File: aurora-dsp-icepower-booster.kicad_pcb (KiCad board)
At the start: 2 copper layers, 180 x 200 mm, 239 parts, among them J1 XLR_IN_1, J10 XLR3_OUT, J11 XLR3_OUT, J12 XLR3_OUT, J13 24V DC, J14 REMOTE 3.5mm, J2 XLR_IN_2, J3 XLR_IN_3, J4 XLR_IN_4, J5 XLR_IN_5, J6 XLR_IN_6, J7 XLR3_OUT, J8 XLR3_OUT, J9 XLR3_OUT, SW1 Gain CH1, SW2 Gain CH2, SW3 Gain CH3, SW4 Gain CH4, SW5 Gain CH5, SW6 Gain CH6, SW7 ALWAYS/REMOTE, U1 LM4562, U10 LM4562, U11 LM4562, U12 LM4562, U13 TEL5-2422, U14 ADP7118ARDZ-11, U15 ADP7182AUJZ-11, U2 LM4562, U3 LM4562, U4 LM4562, U5 LM4562, U6 LM4562, U7 LM4562, U8 LM4562, U9 LM4562

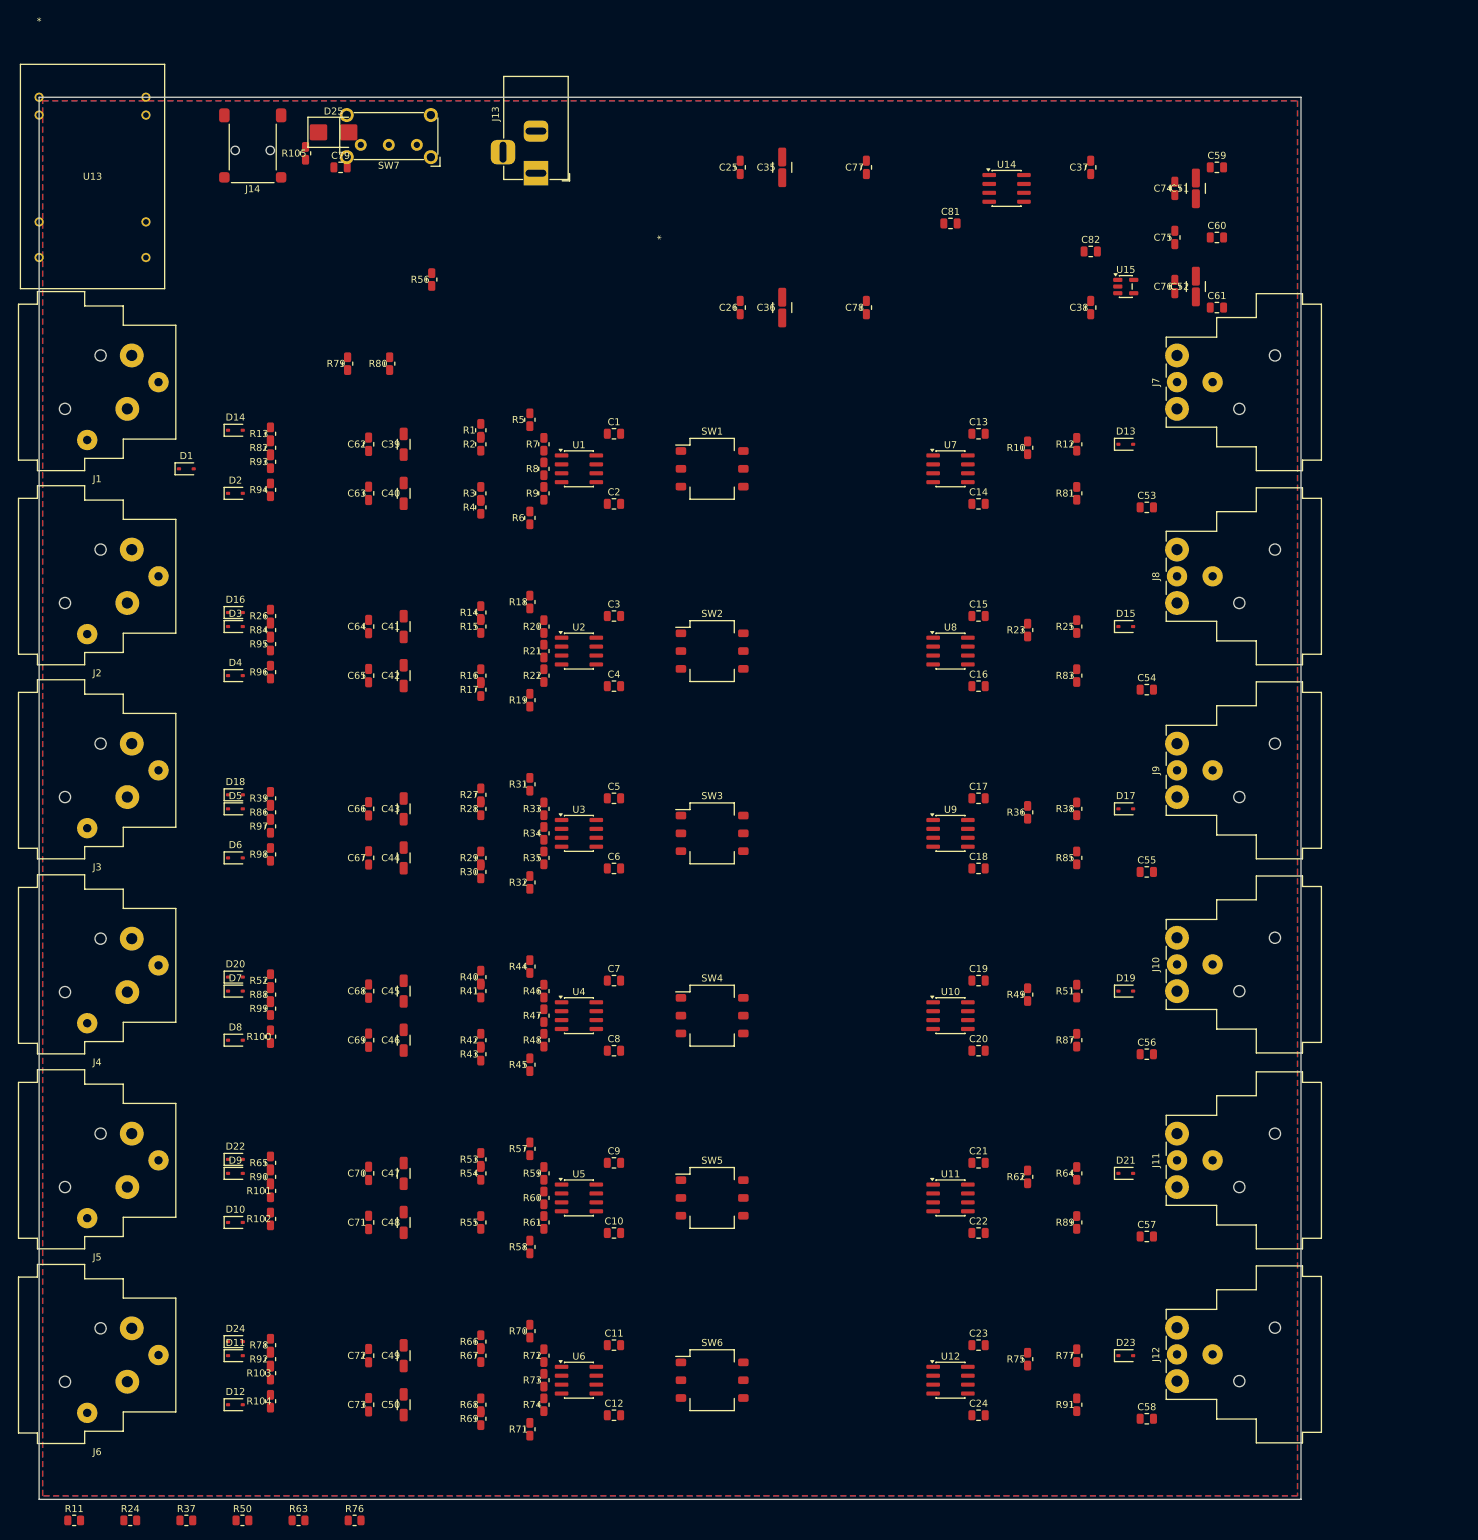
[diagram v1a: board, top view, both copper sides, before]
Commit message: PCB: add build_pcb_v4.py with net-name-driven placement
- 264/264 components placed (0 fallback, 0 skipped)
- Net-name-driven channel+function classification
- Correct netlist refs: J1=barrel, J2=remote, J3-J8=XLR-in,
  J9-J14=XLR-out, SW1=ALWAYS/REMOTE (was wrong in v3)
- U1=TEL5-2422 (was U13 in v3), U14=ADP7118, U15=ADP7182
- IC rules prioritized before passive pattern matching
- Extra .kicad_mod footprints: injection fix for unquoted refs
- DRC: 0 shorts, 18 courtyard/clearance (power zone), 499 unconnected
  (ready for Freerouting)
- Board: 180x200mm, MH1-MH4 mounting holes at corners
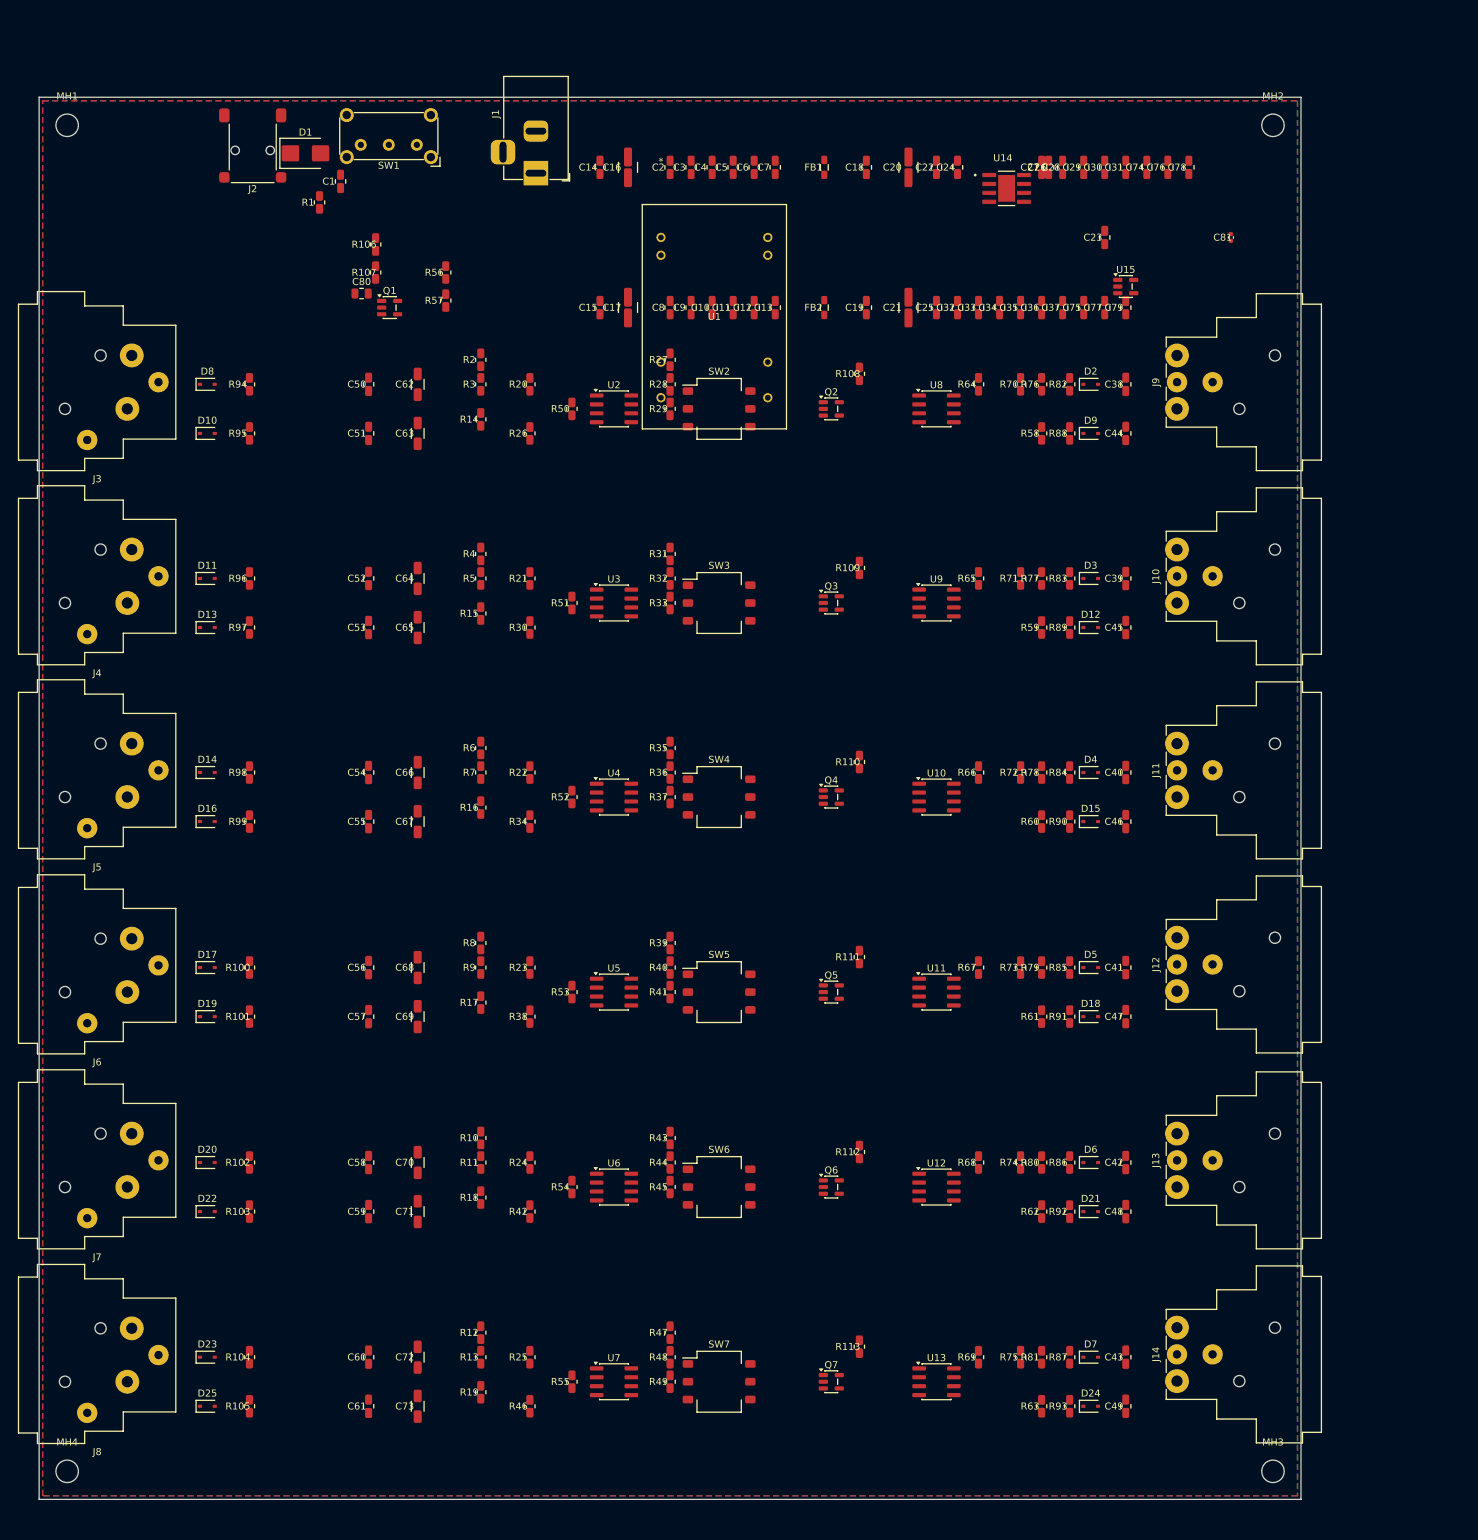
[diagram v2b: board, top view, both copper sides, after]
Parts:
- removed C82: 100nF C0G, Capacitor_SMD:C_0805_2012Metric
- added C27: 100nF C0G, Capacitor_SMD:C_0805_2012Metric, F.Cu at (143.0, 10.0)
- added C28: 100nF C0G, Capacitor_SMD:C_0805_2012Metric, F.Cu at (146.0, 10.0)
- added C29: 100nF C0G, Capacitor_SMD:C_0805_2012Metric, F.Cu at (149.0, 10.0)
- added C30: 100nF C0G, Capacitor_SMD:C_0805_2012Metric, F.Cu at (152.0, 10.0)
- added C31: 100nF C0G, Capacitor_SMD:C_0805_2012Metric, F.Cu at (155.0, 10.0)
- added C32: 100nF C0G, Capacitor_SMD:C_0805_2012Metric, F.Cu at (131.0, 30.0)
- added C33: 100nF C0G, Capacitor_SMD:C_0805_2012Metric, F.Cu at (134.0, 30.0)
- added C34: 100nF C0G, Capacitor_SMD:C_0805_2012Metric, F.Cu at (137.0, 30.0)
- added C80: 10u, Capacitor_SMD:C_0805_2012Metric, F.Cu at (46.0, 28.0)
- added FB1: BLM18PG221, L_0805_2012Metric, F.Cu at (112.0, 10.0)
- added FB2: BLM18PG221, L_0805_2012Metric, F.Cu at (112.0, 30.0)
- added MH1: MountingHole, MountingHole_3.2mm_M3, F.Cu at (4.00, 4.00)
- added MH2: MountingHole, MountingHole_3.2mm_M3, F.Cu at (176.0, 4.00)
- added MH3: MountingHole, MountingHole_3.2mm_M3, F.Cu at (176.0, 196.0)
- added MH4: MountingHole, MountingHole_3.2mm_M3, F.Cu at (4.00, 196.0)
- added Q1: BSS138, Package_TO_SOT_SMD:SOT-23-5, F.Cu at (50.0, 30.0)
- added Q2: BSS138, Package_TO_SOT_SMD:SOT-23-5, F.Cu at (113.0, 44.5)
- added Q3: BSS138, Package_TO_SOT_SMD:SOT-23-5, F.Cu at (113.0, 72.1)
- added Q4: BSS138, Package_TO_SOT_SMD:SOT-23-5, F.Cu at (113.0, 99.8)
- added Q5: BSS138, Package_TO_SOT_SMD:SOT-23-5, F.Cu at (113.0, 127.6)
- added Q6: BSS138, Package_TO_SOT_SMD:SOT-23-5, F.Cu at (113.0, 155.4)
- added Q7: BSS138, Package_TO_SOT_SMD:SOT-23-5, F.Cu at (113.0, 183.2)
- added R106: 10k, Resistor_SMD:R_0805_2012Metric, F.Cu at (48.0, 21.0)
- added R107: 100k, Resistor_SMD:R_0805_2012Metric, F.Cu at (48.0, 25.0)
- added R108: 10k, Resistor_SMD:R_0805_2012Metric, F.Cu at (117.0, 39.5)
- added R109: 10k, Resistor_SMD:R_0805_2012Metric, F.Cu at (117.0, 67.1)
- added R110: 10k, Resistor_SMD:R_0805_2012Metric, F.Cu at (117.0, 94.8)
- added R111: 10k, Resistor_SMD:R_0805_2012Metric, F.Cu at (117.0, 122.6)
- added R112: 10k, Resistor_SMD:R_0805_2012Metric, F.Cu at (117.0, 150.4)
- added R113: 10k, Resistor_SMD:R_0805_2012Metric, F.Cu at (117.0, 178.2)
- C16, C17: value 100nF C0G -> 100uF/25V; footprint Capacitor_SMD:C_0805_2012Metric -> Capacitor_SMD:C_1210_3225Metric
- C20, C21: value 100nF C0G -> 100uF; footprint Capacitor_SMD:C_0805_2012Metric -> Capacitor_SMD:C_1210_3225Metric
- C24, C25, C77, C78, C79: value 100nF C0G -> 10uF X5R
- C35, C36: value 100uF/25V -> 100nF C0G; footprint Capacitor_SMD:C_1210_3225Metric -> Capacitor_SMD:C_0805_2012Metric
- C37, C38: value 10uF X5R -> 100nF C0G
- C39, C40, C41, C42, C43, C44, C45, C46, C47, C48, C49: value 2.2uF C0G -> 100nF C0G; footprint Capacitor_SMD:C_1206_3216Metric -> Capacitor_SMD:C_0805_2012Metric
- C50: value 2.2uF C0G -> 100pF C0G; footprint Capacitor_SMD:C_1206_3216Metric -> Capacitor_SMD:C_0805_2012Metric
- C51, C52: value 100uF -> 100pF C0G; footprint Capacitor_SMD:C_1210_3225Metric -> Capacitor_SMD:C_0805_2012Metric
- C53, C54, C55, C56, C57, C58, C59, C60, C61: value 100nF C0G -> 100pF C0G
- C62, C63, C64: value 100nF C0G -> 2.2uF C0G; footprint Capacitor_SMD:C_0805_2012Metric -> Capacitor_SMD:C_1206_3216Metric
- C65, C66, C67, C68, C69, C70, C71, C72, C73: value 100pF C0G -> 2.2uF C0G; footprint Capacitor_SMD:C_0805_2012Metric -> Capacitor_SMD:C_1206_3216Metric
- C74, C75, C76: value 100pF C0G -> 10uF X5R
- C81: value 100nF C0G -> 22nF C0G; footprint Capacitor_SMD:C_0805_2012Metric -> C_0402_1005Metric
- D1: value PESD5V0S1BL -> SMBJ15CA; footprint Diode_SMD:D_SOD-323 -> Diode_SMD:D_SMB
- D25: value SMBJ15CA -> PESD5V0S1BL; footprint Diode_SMD:D_SMB -> Diode_SMD:D_SOD-323
- J1: value XLR_IN_1 -> 24V DC; footprint Connector_Audio:Jack_XLR_Neutrik_NC3FBH2_Horizontal -> Connector_BarrelJack:BarrelJack_Horizontal
- J13: value 24V DC -> XLR3_OUT; footprint Connector_BarrelJack:BarrelJack_Horizontal -> Connector_Audio:Jack_XLR_Neutrik_NC3MBH_Horizontal
- J14: value REMOTE 3.5mm -> XLR3_OUT; footprint Connector_Audio:Jack_3.5mm_Lumberg_1503_02_Horizontal -> Connector_Audio:Jack_XLR_Neutrik_NC3MBH_Horizontal
- J2: value XLR_IN_2 -> REMOTE 3.5mm; footprint Connector_Audio:Jack_XLR_Neutrik_NC3FBH2_Horizontal -> Connector_Audio:Jack_3.5mm_Lumberg_1503_02_Horizontal
- J3: value XLR_IN_3 -> XLR_IN_1
- J4: value XLR_IN_4 -> XLR_IN_2
- J5: value XLR_IN_5 -> XLR_IN_3
- J6: value XLR_IN_6 -> XLR_IN_4
- J7: value XLR3_OUT -> XLR_IN_5; footprint Connector_Audio:Jack_XLR_Neutrik_NC3MBH_Horizontal -> Connector_Audio:Jack_XLR_Neutrik_NC3FBH2_Horizontal
- J8: value XLR3_OUT -> XLR_IN_6; footprint Connector_Audio:Jack_XLR_Neutrik_NC3MBH_Horizontal -> Connector_Audio:Jack_XLR_Neutrik_NC3FBH2_Horizontal
- R1, R66, R67, R68, R69, R70, R71: value 10k 0.1% -> 10k
- R10, R11, R23, R24, R50: value 10k -> 10k 0.1%
- R105, R62, R63, R76: value 10k -> 47
- R12, R13, R25, R26, R38, R51, R52: value 47 -> 10k 0.1%
- R20, R46, R7: value 30k -> 10k 0.1%
- R21, R34, R8: value 15k -> 10k 0.1%
- R22, R9: value 7.5k -> 10k 0.1%
- R27, R31, R43: value 10k 0.1% -> 30k
- R28, R32, R40, R44: value 10k 0.1% -> 15k
- R29, R41, R45: value 10k 0.1% -> 7.5k
- R33: value 30k -> 7.5k
- R35: value 7.5k -> 30k
- R36: value 10k -> 15k
- R37, R49: value 10k -> 7.5k
- R39: value 47 -> 30k
- R47: value 15k -> 30k
- R48: value 7.5k -> 15k
- R56, R57: value 10k 0.1% -> 100k
- R58: value 10k 0.1% -> 47
- R59: value 30k -> 47
- R60: value 15k -> 47
- R61: value 7.5k -> 47
- R64, R65: value 47 -> 10k
- R72: value 30k -> 10k
- R73: value 15k -> 10k
- R74: value 7.5k -> 10k
- R79, R80: value 100k -> 47
- R81: value 10 -> 47
- R93: value 47 -> 10
- SW1: value Gain CH1 -> ALWAYS/REMOTE; footprint Button_Switch_SMD:SW_DIP_SPSTx03_Slide_Omron_A6S-310x_W8.9mm_P2.54mm -> Button_Switch_THT:SW_E-Switch_EG1224_SPDT_Angled
- SW2: value Gain CH2 -> Gain CH1
- SW3: value Gain CH3 -> Gain CH2
- SW4: value Gain CH4 -> Gain CH3
- SW5: value Gain CH5 -> Gain CH4
- SW6: value Gain CH6 -> Gain CH5
- SW7: value ALWAYS/REMOTE -> Gain CH6; footprint Button_Switch_THT:SW_E-Switch_EG1224_SPDT_Angled -> Button_Switch_SMD:SW_DIP_SPSTx03_Slide_Omron_A6S-310x_W8.9mm_P2.54mm
- U1: value LM4562 -> TEL5-2422; footprint Package_SO:SOIC-8_3.9x4.9mm_P1.27mm -> TEL5_DUAL_TRP
- U13: value TEL5-2422 -> LM4562; footprint TEL5_DUAL_TRP -> Package_SO:SOIC-8_3.9x4.9mm_P1.27mm
- U14: footprint Package_SO:SOIC-8_3.9x4.9mm_P1.27mm -> SOIC127P600X175-9N
- moved U13 223.5 mm to (128.0, 183.2)
- moved J14 221.5 mm to (162.3, 183.1), turned to 90 degrees
- moved C60 200.4 mm to (47.0, 179.7), turned to 90 degrees
- moved C61 198.0 mm to (47.0, 186.7), turned to 90 degrees
- moved C59 191.9 mm to (47.0, 158.9), turned to 90 degrees
- moved R76 189.4 mm to (143.0, 41.0), turned to 90 degrees
- moved J8 186.4 mm to (12.6, 183.2), turned to 180 degrees
- moved J7 186.4 mm to (12.6, 155.4), turned to 180 degrees
- moved D25 182.6 mm to (24.0, 186.7)
- moved SW7 181.6 mm to (97.0, 183.2), turned to 0 degrees
- moved R105 178.9 mm to (30.0, 186.7)
- moved C24 178.0 mm to (131.0, 10.0), turned to 90 degrees
- moved R93 176.5 mm to (147.0, 186.7)
- moved J13 171.1 mm to (162.3, 155.4), turned to 90 degrees
- moved R50 165.4 mm to (76.0, 44.5), turned to 90 degrees
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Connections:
- C1 pad 1: /GND -> /REMOTE_FILT
- C1 pad 2: /V+ -> GND
- C10 pad 1: /GND -> GND
- C11 pad 1: /GND -> GND
- C11 pad 2: /V+ -> /V-
- C12 pad 1: /V- -> GND
- C12 pad 2: /GND -> /V-
- C13 pad 1: /GND -> GND
- C13 pad 2: /V+ -> /V-
- C14 pad 1: /GND -> GND
- C14 pad 2: /V- -> /+12V_RAW
- C15 pad 1: /GND -> /-12V_RAW
- C15 pad 2: /V+ -> GND
- C16 pad 1: /V- -> GND
- C16 pad 2: /GND -> /+12V_RAW
- C17 pad 1: /GND -> /-12V_RAW
- C17 pad 2: /V+ -> GND
- C18 pad 1: /GND -> GND
- C18 pad 2: /V- -> /+12V
- C19 pad 1: /GND -> /-12V
- C19 pad 2: /V+ -> GND
- C2 pad 1: /GND -> GND
- C2 pad 2: /V- -> /V+
- C20 pad 1: /V- -> GND
- C20 pad 2: /GND -> /V+
- C21 pad 1: /GND -> /V-
- C21 pad 2: /V+ -> GND
- C22 pad 1: /GND -> /V+
- C22 pad 2: /V- -> GND
- C23 pad 1: /GND -> /NR_U15
- C23 pad 2: /V+ -> GND
- C24 pad 1: /V- -> GND
- C24 pad 2: /GND -> /V+
- C25 pad 1: /GND -> /V-
- C25 pad 2: /+12V -> GND
- C26 pad 1: /-12V -> GND
- C26 pad 2: /GND -> /V+
- C3 pad 1: /GND -> GND
- C35 pad 1: /GND -> /V-
- C35 pad 2: /+12V -> GND
- C36 pad 1: /-12V -> /V-
- C36 pad 2: /GND -> GND
- C37 pad 1: /GND -> /V-
- C37 pad 2: /V+ -> GND
- C38 pad 1: /V- -> /CH1_OUT_PROT_HOT
- C38 pad 2: /GND -> GND
- C39 pad 1: (no net) -> /CH2_OUT_PROT_HOT
- C39 pad 2: /CH1_HOT_IN -> GND
- C4 pad 1: /V- -> GND
- C4 pad 2: /GND -> /V+
- C40 pad 1: (no net) -> /CH3_OUT_PROT_HOT
- C40 pad 2: /CH1_COLD_IN -> GND
- C41 pad 1: (no net) -> /CH4_OUT_PROT_HOT
- C41 pad 2: /CH2_HOT_IN -> GND
- C42 pad 1: (no net) -> /CH5_OUT_PROT_HOT
- C42 pad 2: /CH2_COLD_IN -> GND
- C43 pad 1: (no net) -> /CH6_OUT_PROT_HOT
- C43 pad 2: /CH3_HOT_IN -> GND
- C44 pad 1: (no net) -> /CH1_OUT_PROT_COLD
- C44 pad 2: /CH3_COLD_IN -> GND
- C45 pad 1: (no net) -> /CH2_OUT_PROT_COLD
- C45 pad 2: /CH4_HOT_IN -> GND
- C46 pad 1: (no net) -> /CH3_OUT_PROT_COLD
- C46 pad 2: /CH4_COLD_IN -> GND
- C47 pad 1: (no net) -> /CH4_OUT_PROT_COLD
- C47 pad 2: /CH5_HOT_IN -> GND
- C48 pad 1: (no net) -> /CH5_OUT_PROT_COLD
- C48 pad 2: /CH5_COLD_IN -> GND
- C49 pad 1: (no net) -> /CH6_OUT_PROT_COLD
- C49 pad 2: /CH6_HOT_IN -> GND
- C5 pad 1: /GND -> GND
- C50 pad 1: (no net) -> /CH1_EMI_HOT
- C50 pad 2: /CH6_COLD_IN -> GND
- C51 pad 1: /GND -> /CH1_EMI_COLD
- C51 pad 2: /GND -> GND
- C52 pad 1: /GND -> /CH2_EMI_HOT
- C52 pad 2: /GND -> GND
- C53 pad 1: (no net) -> /CH2_EMI_COLD
- C53 pad 2: /GND -> GND
- C54 pad 1: (no net) -> /CH3_EMI_HOT
- C54 pad 2: /GND -> GND
- C55 pad 1: (no net) -> /CH3_EMI_COLD
- C55 pad 2: /GND -> GND
- C56 pad 1: (no net) -> /CH4_EMI_HOT
- C56 pad 2: /GND -> GND
- C57 pad 1: (no net) -> /CH4_EMI_COLD
- C57 pad 2: /GND -> GND
- C58 pad 1: (no net) -> /CH5_EMI_HOT
- C58 pad 2: /GND -> GND
- C59 pad 1: (no net) -> /CH5_EMI_COLD
- C59 pad 2: /GND -> GND
- C6 pad 1: /GND -> GND
- C6 pad 2: /V- -> /V+
- C60 pad 1: (no net) -> /CH6_EMI_HOT
- C60 pad 2: /GND -> GND
- C61 pad 1: (no net) -> /CH6_EMI_COLD
- C61 pad 2: /GND -> GND
- C62 pad 1: (no net) -> /CH1_EMI_HOT
- C62 pad 2: /GND -> /CH1_HOT_IN
- C63 pad 1: (no net) -> /CH1_EMI_COLD
- C63 pad 2: /GND -> /CH1_COLD_IN
- C64 pad 1: (no net) -> /CH2_EMI_HOT
- C64 pad 2: /GND -> /CH2_HOT_IN
- C65 pad 1: (no net) -> /CH2_EMI_COLD
- C65 pad 2: /GND -> /CH2_COLD_IN
- C66 pad 1: (no net) -> /CH3_EMI_HOT
- C66 pad 2: /GND -> /CH3_HOT_IN
- C67 pad 1: (no net) -> /CH3_EMI_COLD
- C67 pad 2: /GND -> /CH3_COLD_IN
- C68 pad 1: (no net) -> /CH4_EMI_HOT
- C68 pad 2: /GND -> /CH4_HOT_IN
- C69 pad 1: (no net) -> /CH4_EMI_COLD
- C69 pad 2: /GND -> /CH4_COLD_IN
- C7 pad 1: /GND -> GND
- C70 pad 1: (no net) -> /CH5_EMI_HOT
- C70 pad 2: /GND -> /CH5_HOT_IN
- C71 pad 1: (no net) -> /CH5_EMI_COLD
- C71 pad 2: /GND -> /CH5_COLD_IN
- C72 pad 1: (no net) -> /CH6_EMI_HOT
- C72 pad 2: /GND -> /CH6_HOT_IN
- C73 pad 1: (no net) -> /CH6_EMI_COLD
- C73 pad 2: /GND -> /CH6_COLD_IN
- C74 pad 1: (no net) -> GND
- C74 pad 2: /GND -> /V+
- C75 pad 1: (no net) -> /V-
- C75 pad 2: /GND -> GND
- C76 pad 1: (no net) -> GND
- C76 pad 2: /GND -> /V+
- C77 pad 1: /GND -> /V-
- C77 pad 2: /+12V -> GND
- C78 pad 1: /-12V -> GND
- C78 pad 2: /GND -> /V+
- C79 pad 1: /REMOTE_FILT -> /V-
- C79 pad 2: /GND -> GND
- C8 pad 1: /V- -> GND
- C8 pad 2: /GND -> /V-
- C81 pad 2: /GND -> GND
- C9 pad 1: /GND -> GND
- C9 pad 2: /V+ -> /V-
- D1 pad 1: /GND -> /REMOTE_IN
- D1 pad 2: /CH1_HOT_RAW -> GND
- D10 pad 1: /GND -> GND
- D10 pad 2: /CH5_COLD_RAW -> /CH1_COLD_RAW
- D11 pad 1: /GND -> GND
- D11 pad 2: /CH6_HOT_RAW -> /CH2_HOT_RAW
- D12 pad 1: /GND -> GND
- D12 pad 2: /CH6_COLD_RAW -> /CH2_OUT_COLD
- D13 pad 1: /GND -> GND
- D13 pad 2: /CH1_OUT_HOT -> /CH2_COLD_RAW
- D14 pad 1: /GND -> GND
- D14 pad 2: /CH1_HOT_RAW -> /CH3_HOT_RAW
- D15 pad 1: /GND -> GND
- D15 pad 2: /CH2_OUT_HOT -> /CH3_OUT_COLD
- D16 pad 1: /GND -> GND
- D16 pad 2: /CH2_HOT_RAW -> /CH3_COLD_RAW
- D17 pad 1: /GND -> GND
- D17 pad 2: /CH3_OUT_HOT -> /CH4_HOT_RAW
- D18 pad 1: /GND -> GND
- D18 pad 2: /CH3_HOT_RAW -> /CH4_OUT_COLD
- D19 pad 1: /GND -> GND
- D19 pad 2: /CH4_OUT_HOT -> /CH4_COLD_RAW
- D2 pad 1: /GND -> GND
- D2 pad 2: /CH1_COLD_RAW -> /CH1_OUT_HOT
- D20 pad 1: /GND -> GND
- D20 pad 2: /CH4_HOT_RAW -> /CH5_HOT_RAW
- D21 pad 1: /GND -> GND
- D21 pad 2: /CH5_OUT_HOT -> /CH5_OUT_COLD
- D22 pad 1: /GND -> GND
- D22 pad 2: /CH5_HOT_RAW -> /CH5_COLD_RAW
- D23 pad 1: /GND -> GND
- D23 pad 2: /CH6_OUT_HOT -> /CH6_HOT_RAW
- D24 pad 1: /GND -> GND
- D24 pad 2: /CH6_HOT_RAW -> /CH6_OUT_COLD
- D25 pad 1: /REMOTE_IN -> GND
- D25 pad 2: /GND -> /CH6_COLD_RAW
- D3 pad 1: /GND -> GND
- D3 pad 2: /CH2_HOT_RAW -> /CH2_OUT_HOT
- D4 pad 1: /GND -> GND
- D4 pad 2: /CH2_COLD_RAW -> /CH3_OUT_HOT
- D5 pad 1: /GND -> GND
- D5 pad 2: /CH3_HOT_RAW -> /CH4_OUT_HOT
- D6 pad 1: /GND -> GND
- D6 pad 2: /CH3_COLD_RAW -> /CH5_OUT_HOT
- D7 pad 1: /GND -> GND
- D7 pad 2: /CH4_HOT_RAW -> /CH6_OUT_HOT
- D8 pad 1: /GND -> GND
- D8 pad 2: /CH4_COLD_RAW -> /CH1_HOT_RAW
- D9 pad 1: /GND -> GND
- D9 pad 2: /CH5_HOT_RAW -> /CH1_OUT_COLD
- J1 pad 1: /GND -> /+24V_IN
- J1 pad 2: /CH1_HOT_RAW -> GND
- J10 pad 1: /GND -> GND
- J10 pad 2: /CH4_OUT_HOT -> /CH2_OUT_HOT
- J10 pad 3: (no net) -> /CH2_OUT_COLD
- J11 pad 1: /GND -> GND
- J11 pad 2: /CH5_OUT_HOT -> /CH3_OUT_HOT
- J11 pad 3: (no net) -> /CH3_OUT_COLD
- J12 pad 1: /GND -> GND
- J12 pad 2: /CH6_OUT_HOT -> /CH4_OUT_HOT
- J12 pad 3: (no net) -> /CH4_OUT_COLD
- J13 pad 1: /+24V_IN -> GND
- J13 pad 2: /GND -> /CH5_OUT_HOT
- J13 pad 3: (no net) -> /CH5_OUT_COLD
- J3 pad 1: /GND -> GND
- J3 pad 2: /CH3_HOT_RAW -> /CH1_HOT_RAW
- J3 pad 3: (no net) -> /CH1_COLD_RAW
- J3 pad G: (no net) -> GND
- J4 pad 1: /GND -> GND
- J4 pad 2: /CH4_HOT_RAW -> /CH2_HOT_RAW
- J4 pad 3: (no net) -> /CH2_COLD_RAW
- J4 pad G: (no net) -> GND
- J5 pad 1: /GND -> GND
- J5 pad 2: /CH5_HOT_RAW -> /CH3_HOT_RAW
- J5 pad 3: (no net) -> /CH3_COLD_RAW
- J5 pad G: (no net) -> GND
- J6 pad 1: /GND -> GND
- J6 pad 2: /CH6_HOT_RAW -> /CH4_HOT_RAW
- J6 pad 3: (no net) -> /CH4_COLD_RAW
- J6 pad G: (no net) -> GND
- J7 pad 1: /GND -> GND
- J7 pad 2: /CH1_OUT_HOT -> /CH5_HOT_RAW
- J7 pad 3: (no net) -> /CH5_COLD_RAW
- J7 pad G: (no net) -> GND
- J8 pad 1: /GND -> GND
- J8 pad 2: /CH2_OUT_HOT -> /CH6_HOT_RAW
- J8 pad 3: (no net) -> /CH6_COLD_RAW
- J8 pad G: (no net) -> GND
- J9 pad 1: /GND -> GND
- J9 pad 2: /CH3_OUT_HOT -> /CH1_OUT_HOT
- J9 pad 3: (no net) -> /CH1_OUT_COLD
- R1 pad 1: (no net) -> /REMOTE_IN
- R1 pad 2: /CH1_HOT_IN -> /REMOTE_FILT
- R10 pad 1: (no net) -> GND
- R10 pad 2: /CH1_GAIN_OUT -> /CH5_HOT_IN
- R100 pad 1: /CH4_COLD_RAW -> /CH4_HOT_RAW
- R100 pad 2: (no net) -> /CH4_EMI_HOT
- R101 pad 1: /CH5_HOT_RAW -> /CH4_COLD_RAW
- R101 pad 2: (no net) -> /CH4_EMI_COLD
- R102 pad 1: /CH5_COLD_RAW -> /CH5_HOT_RAW
- R102 pad 2: (no net) -> /CH5_EMI_HOT
- R103 pad 1: /CH6_HOT_RAW -> /CH5_COLD_RAW
- R103 pad 2: (no net) -> /CH5_EMI_COLD
- R104 pad 1: /CH6_COLD_RAW -> /CH6_HOT_RAW
- R104 pad 2: (no net) -> /CH6_EMI_HOT
- R105 pad 1: /REMOTE_IN -> /CH6_COLD_RAW
- R105 pad 2: /REMOTE_FILT -> /CH6_EMI_COLD
- R11 pad 1: (no net) -> /CH5_INV_IN
- R11 pad 2: (no net) -> /CH5_COLD_IN
- R12 pad 1: (no net) -> GND
- R12 pad 2: /CH1_OUT_HOT -> /CH6_HOT_IN
- R13 pad 1: (no net) -> /CH6_INV_IN
- R13 pad 2: /CH1_HOT_RAW -> /CH6_COLD_IN
- R14 pad 1: /CH2_HOT_IN -> GND
- R14 pad 2: /CH2_HOT_IN -> /CH1_INV_IN
- R15 pad 1: /CH2_HOT_IN -> GND
- R15 pad 2: (no net) -> /CH2_INV_IN
- R16 pad 1: (no net) -> GND
- R16 pad 2: /CH2_COLD_IN -> /CH3_INV_IN
- R17 pad 1: /GND -> GND
- R17 pad 2: (no net) -> /CH4_INV_IN
- R18 pad 1: /CH2_SUMNODE -> GND
- R18 pad 2: /CH2_RX_OUT -> /CH5_INV_IN
- R19 pad 1: /CH2_SUMNODE -> GND
- R19 pad 2: /CH2_GAIN_OUT -> /CH6_INV_IN
- R2 pad 1: /CH1_HOT_IN -> GND
- R2 pad 2: (no net) -> /CH1_HOT_IN
- R20 pad 1: (no net) -> /CH1_INV_IN
- R20 pad 2: /CH2_SUMNODE -> /CH1_RX_OUT
- R21 pad 1: (no net) -> /CH2_INV_IN
- R21 pad 2: /CH2_SUMNODE -> /CH2_RX_OUT
- R22 pad 1: (no net) -> /CH3_INV_IN
- R22 pad 2: /CH2_SUMNODE -> /CH3_RX_OUT
- R23 pad 1: (no net) -> /CH4_INV_IN
- R23 pad 2: /CH2_GAIN_OUT -> /CH4_RX_OUT
- R24 pad 1: (no net) -> /CH5_INV_IN
- R24 pad 2: (no net) -> /CH5_RX_OUT
- R25 pad 1: (no net) -> /CH6_INV_IN
- R25 pad 2: /CH2_OUT_HOT -> /CH6_RX_OUT
- R26 pad 1: (no net) -> /CH1_SUMNODE
- R26 pad 2: /CH2_HOT_RAW -> /CH1_RX_OUT
- R27 pad 1: /CH3_HOT_IN -> /CH1_SW_OUT_1
- R27 pad 2: /CH3_HOT_IN -> /CH1_SUMNODE
- R28 pad 1: /CH3_HOT_IN -> /CH1_SW_OUT_2
- R28 pad 2: (no net) -> /CH1_SUMNODE
- R29 pad 1: (no net) -> /CH1_SW_OUT_3
- R29 pad 2: /CH3_COLD_IN -> /CH1_SUMNODE
- R3 pad 1: (no net) -> /CH1_INV_IN
- R30 pad 1: /GND -> /CH2_SUMNODE
- R30 pad 2: (no net) -> /CH2_RX_OUT
- R31 pad 1: /CH3_SUMNODE -> /CH2_SW_OUT_1
- R31 pad 2: /CH3_RX_OUT -> /CH2_SUMNODE
- R32 pad 1: /CH3_SUMNODE -> /CH2_SW_OUT_2
- R32 pad 2: /CH3_GAIN_OUT -> /CH2_SUMNODE
- R33 pad 1: (no net) -> /CH2_SW_OUT_3
- R33 pad 2: /CH3_SUMNODE -> /CH2_SUMNODE
- R34 pad 1: (no net) -> /CH3_SUMNODE
- R34 pad 2: /CH3_SUMNODE -> /CH3_RX_OUT
- R35 pad 1: (no net) -> /CH3_SW_OUT_1
- R36 pad 1: (no net) -> /CH3_SW_OUT_2
- R36 pad 2: /CH3_GAIN_OUT -> /CH3_SUMNODE
- R37 pad 1: (no net) -> /CH3_SW_OUT_3
- R37 pad 2: (no net) -> /CH3_SUMNODE
- R38 pad 1: (no net) -> /CH4_SUMNODE
- R38 pad 2: /CH3_OUT_HOT -> /CH4_RX_OUT
- R39 pad 1: (no net) -> /CH4_SW_OUT_1
- R39 pad 2: /CH3_HOT_RAW -> /CH4_SUMNODE
- R4 pad 1: /GND -> GND
- R4 pad 2: (no net) -> /CH2_HOT_IN
- R40 pad 1: /CH4_HOT_IN -> /CH4_SW_OUT_2
- R40 pad 2: /CH4_HOT_IN -> /CH4_SUMNODE
- R41 pad 1: /CH4_HOT_IN -> /CH4_SW_OUT_3
- R41 pad 2: (no net) -> /CH4_SUMNODE
- R42 pad 1: (no net) -> /CH5_SUMNODE
- R42 pad 2: /CH4_COLD_IN -> /CH5_RX_OUT
- R43 pad 1: /GND -> /CH5_SW_OUT_1
- R43 pad 2: (no net) -> /CH5_SUMNODE
- R44 pad 1: /CH4_SUMNODE -> /CH5_SW_OUT_2
- R44 pad 2: /CH4_RX_OUT -> /CH5_SUMNODE
- R45 pad 1: /CH4_SUMNODE -> /CH5_SW_OUT_3
- R45 pad 2: /CH4_GAIN_OUT -> /CH5_SUMNODE
- R46 pad 1: (no net) -> /CH6_SUMNODE
- R46 pad 2: /CH4_SUMNODE -> /CH6_RX_OUT
- R47 pad 1: (no net) -> /CH6_SW_OUT_1
- R47 pad 2: /CH4_SUMNODE -> /CH6_SUMNODE
- R48 pad 1: (no net) -> /CH6_SW_OUT_2
- R48 pad 2: /CH4_SUMNODE -> /CH6_SUMNODE
- R49 pad 1: (no net) -> /CH6_SW_OUT_3
- R49 pad 2: /CH4_GAIN_OUT -> /CH6_SUMNODE
- R5 pad 1: /CH1_SUMNODE -> /CH2_INV_IN
- R5 pad 2: /CH1_RX_OUT -> /CH2_COLD_IN
- R50 pad 1: (no net) -> /CH1_SUMNODE
- R50 pad 2: (no net) -> /CH1_GAIN_OUT
- R51 pad 1: (no net) -> /CH2_SUMNODE
- R51 pad 2: /CH4_OUT_HOT -> /CH2_GAIN_OUT
- R52 pad 1: (no net) -> /CH3_SUMNODE
- R52 pad 2: /CH4_HOT_RAW -> /CH3_GAIN_OUT
- R53 pad 1: /CH5_HOT_IN -> /CH4_SUMNODE
- R53 pad 2: /CH5_HOT_IN -> /CH4_GAIN_OUT
- R54 pad 1: /CH5_HOT_IN -> /CH5_SUMNODE
- R54 pad 2: (no net) -> /CH5_GAIN_OUT
- R55 pad 1: (no net) -> /CH6_SUMNODE
- R55 pad 2: /CH5_COLD_IN -> /CH6_GAIN_OUT
- R56 pad 1: /GND -> /EN_CTRL
- R56 pad 2: (no net) -> /V+
- R57 pad 1: /CH5_SUMNODE -> /EN_CTRL
- R57 pad 2: /CH5_RX_OUT -> GND
- R58 pad 1: /CH5_SUMNODE -> /CH1_BUF_DRIVE
- R58 pad 2: /CH5_GAIN_OUT -> /CH1_OUT_COLD
- R59 pad 1: (no net) -> /CH2_BUF_DRIVE
- R59 pad 2: /CH5_SUMNODE -> /CH2_OUT_COLD
- R6 pad 1: /CH1_SUMNODE -> GND
- R6 pad 2: /CH1_GAIN_OUT -> /CH3_HOT_IN
- R60 pad 1: (no net) -> /CH3_BUF_DRIVE
- R60 pad 2: /CH5_SUMNODE -> /CH3_OUT_COLD
- R61 pad 1: (no net) -> /CH4_BUF_DRIVE
- R61 pad 2: /CH5_SUMNODE -> /CH4_OUT_COLD
- R62 pad 1: (no net) -> /CH5_BUF_DRIVE
- R62 pad 2: /CH5_GAIN_OUT -> /CH5_OUT_COLD
- R63 pad 1: (no net) -> /CH6_BUF_DRIVE
- R63 pad 2: (no net) -> /CH6_OUT_COLD
- R64 pad 1: (no net) -> /CH1_GAIN_FB
- R64 pad 2: /CH5_OUT_HOT -> /CH1_GAIN_OUT
- R65 pad 1: (no net) -> /CH2_GAIN_FB
- R65 pad 2: /CH5_HOT_RAW -> /CH2_GAIN_OUT
- R66 pad 1: /CH6_HOT_IN -> /CH3_GAIN_FB
- R66 pad 2: /CH6_HOT_IN -> /CH3_GAIN_OUT
- R67 pad 1: /CH6_HOT_IN -> /CH4_GAIN_FB
- R67 pad 2: (no net) -> /CH4_GAIN_OUT
- R68 pad 1: (no net) -> /CH5_GAIN_FB
- R68 pad 2: /CH6_COLD_IN -> /CH5_GAIN_OUT
- R69 pad 1: /GND -> /CH6_GAIN_FB
- R69 pad 2: (no net) -> /CH6_GAIN_OUT
- R7 pad 1: (no net) -> /CH3_INV_IN
- R7 pad 2: /CH1_SUMNODE -> /CH3_COLD_IN
- R70 pad 1: /CH6_SUMNODE -> /CH1_GAIN_FB
- R70 pad 2: /CH6_RX_OUT -> /CH1_OUT_DRIVE
- R71 pad 1: /CH6_SUMNODE -> /CH2_GAIN_FB
- R71 pad 2: /CH6_GAIN_OUT -> /CH2_OUT_DRIVE
- R72 pad 1: (no net) -> /CH3_GAIN_FB
- R72 pad 2: /CH6_SUMNODE -> /CH3_OUT_DRIVE
- R73 pad 1: (no net) -> /CH4_GAIN_FB
- R73 pad 2: /CH6_SUMNODE -> /CH4_OUT_DRIVE
- R74 pad 1: (no net) -> /CH5_GAIN_FB
- R74 pad 2: /CH6_SUMNODE -> /CH5_OUT_DRIVE
- R75 pad 1: (no net) -> /CH6_GAIN_FB
- R75 pad 2: /CH6_GAIN_OUT -> /CH6_OUT_DRIVE
- R76 pad 1: (no net) -> /CH1_OUT_DRIVE
- R76 pad 2: (no net) -> /CH1_OUT_HOT
- R77 pad 1: (no net) -> /CH2_OUT_DRIVE
- R77 pad 2: /CH6_OUT_HOT -> /CH2_OUT_HOT
- R78 pad 1: (no net) -> /CH3_OUT_DRIVE
- R78 pad 2: /CH6_HOT_RAW -> /CH3_OUT_HOT
- R79 pad 1: /EN_CTRL -> /CH4_OUT_DRIVE
- R79 pad 2: /GND -> /CH4_OUT_HOT
- R8 pad 1: (no net) -> GND
- R8 pad 2: /CH1_SUMNODE -> /CH4_HOT_IN
- R80 pad 1: /EN_CTRL -> /CH5_OUT_DRIVE
- R80 pad 2: /GND -> /CH5_OUT_HOT
- R81 pad 1: /CH1_OUT_HOT -> /CH6_OUT_DRIVE
- R81 pad 2: (no net) -> /CH6_OUT_HOT
- R82 pad 1: /CH1_HOT_RAW -> /CH1_OUT_HOT
- R82 pad 2: (no net) -> /CH1_OUT_PROT_HOT
- R83 pad 2: (no net) -> /CH2_OUT_PROT_HOT
- R84 pad 1: /CH2_HOT_RAW -> /CH3_OUT_HOT
- R84 pad 2: (no net) -> /CH3_OUT_PROT_HOT
- R85 pad 1: /CH3_OUT_HOT -> /CH4_OUT_HOT
- R85 pad 2: (no net) -> /CH4_OUT_PROT_HOT
- R86 pad 1: /CH3_HOT_RAW -> /CH5_OUT_HOT
- R86 pad 2: (no net) -> /CH5_OUT_PROT_HOT
- R87 pad 1: /CH4_OUT_HOT -> /CH6_OUT_HOT
- R87 pad 2: (no net) -> /CH6_OUT_PROT_HOT
- R88 pad 1: /CH4_HOT_RAW -> /CH1_OUT_COLD
- R88 pad 2: (no net) -> /CH1_OUT_PROT_COLD
- R89 pad 1: /CH5_OUT_HOT -> /CH2_OUT_COLD
- R89 pad 2: (no net) -> /CH2_OUT_PROT_COLD
- R9 pad 1: (no net) -> /CH4_INV_IN
- R9 pad 2: /CH1_SUMNODE -> /CH4_COLD_IN
- R90 pad 1: /CH5_HOT_RAW -> /CH3_OUT_COLD
- R90 pad 2: (no net) -> /CH3_OUT_PROT_COLD
- R91 pad 1: /CH6_OUT_HOT -> /CH4_OUT_COLD
- R91 pad 2: (no net) -> /CH4_OUT_PROT_COLD
- R92 pad 1: /CH6_HOT_RAW -> /CH5_OUT_COLD
- R92 pad 2: (no net) -> /CH5_OUT_PROT_COLD
- R93 pad 1: /CH1_HOT_RAW -> /CH6_OUT_COLD
- R93 pad 2: (no net) -> /CH6_OUT_PROT_COLD
- R94 pad 1: /CH1_COLD_RAW -> /CH1_HOT_RAW
- R94 pad 2: (no net) -> /CH1_EMI_HOT
- R95 pad 1: /CH2_HOT_RAW -> /CH1_COLD_RAW
- R95 pad 2: (no net) -> /CH1_EMI_COLD
- R96 pad 1: /CH2_COLD_RAW -> /CH2_HOT_RAW
- R96 pad 2: (no net) -> /CH2_EMI_HOT
- R97 pad 1: /CH3_HOT_RAW -> /CH2_COLD_RAW
- R97 pad 2: (no net) -> /CH2_EMI_COLD
- R98 pad 1: /CH3_COLD_RAW -> /CH3_HOT_RAW
- R98 pad 2: (no net) -> /CH3_EMI_HOT
- R99 pad 1: /CH4_HOT_RAW -> /CH3_COLD_RAW
- R99 pad 2: (no net) -> /CH3_EMI_COLD
- SW1 pad 1: /CH1_RX_OUT -> /+12V
- SW1 pad 2: /CH1_RX_OUT -> /EN_CTRL
- SW1 pad 3: /CH1_RX_OUT -> /REMOTE_FILT
- SW2 pad 1: /CH2_RX_OUT -> /CH1_RX_OUT
- SW2 pad 2: /CH2_RX_OUT -> /CH1_RX_OUT
- SW2 pad 3: /CH2_RX_OUT -> /CH1_RX_OUT
- SW2 pad 4: (no net) -> /CH1_SW_OUT_3
- SW2 pad 5: (no net) -> /CH1_SW_OUT_2
- SW2 pad 6: (no net) -> /CH1_SW_OUT_1
- SW3 pad 1: /CH3_RX_OUT -> /CH2_RX_OUT
- SW3 pad 2: /CH3_RX_OUT -> /CH2_RX_OUT
- SW3 pad 3: /CH3_RX_OUT -> /CH2_RX_OUT
- SW3 pad 4: (no net) -> /CH2_SW_OUT_3
- SW3 pad 5: (no net) -> /CH2_SW_OUT_2
- SW3 pad 6: (no net) -> /CH2_SW_OUT_1
- SW4 pad 1: /CH4_RX_OUT -> /CH3_RX_OUT
- SW4 pad 2: /CH4_RX_OUT -> /CH3_RX_OUT
- SW4 pad 3: /CH4_RX_OUT -> /CH3_RX_OUT
- SW4 pad 4: (no net) -> /CH3_SW_OUT_3
- SW4 pad 5: (no net) -> /CH3_SW_OUT_2
- SW4 pad 6: (no net) -> /CH3_SW_OUT_1
- SW5 pad 1: /CH5_RX_OUT -> /CH4_RX_OUT
- SW5 pad 2: /CH5_RX_OUT -> /CH4_RX_OUT
- SW5 pad 3: /CH5_RX_OUT -> /CH4_RX_OUT
- SW5 pad 4: (no net) -> /CH4_SW_OUT_3
- SW5 pad 5: (no net) -> /CH4_SW_OUT_2
- SW5 pad 6: (no net) -> /CH4_SW_OUT_1
- SW6 pad 1: /CH6_RX_OUT -> /CH5_RX_OUT
- SW6 pad 2: /CH6_RX_OUT -> /CH5_RX_OUT
- SW6 pad 3: /CH6_RX_OUT -> /CH5_RX_OUT
- SW6 pad 4: (no net) -> /CH5_SW_OUT_3
- SW6 pad 5: (no net) -> /CH5_SW_OUT_2
- SW6 pad 6: (no net) -> /CH5_SW_OUT_1
- SW7 pad 1: /+12V -> /CH6_RX_OUT
- SW7 pad 2: /EN_CTRL -> /CH6_RX_OUT
- SW7 pad 3: /REMOTE_FILT -> /CH6_RX_OUT
- U1 pad 2: (no net) -> GND
- U1 pad 3: /CH1_HOT_IN -> GND
- U10 pad 1: (no net) -> /CH3_BUF_DRIVE
- U10 pad 2: /CH4_GAIN_OUT -> /CH3_BUF_DRIVE
- U10 pad 3: (no net) -> /CH3_GAIN_OUT
- U10 pad 4: (no net) -> /V-
- U10 pad 5: (no net) -> GND
- U10 pad 6: /GND -> /CH3_GAIN_FB
- U10 pad 7: (no net) -> /CH3_OUT_DRIVE
- U10 pad 8: (no net) -> /V+
- U11 pad 1: (no net) -> /CH4_BUF_DRIVE
- U11 pad 2: /CH5_GAIN_OUT -> /CH4_BUF_DRIVE
- U11 pad 3: (no net) -> /CH4_GAIN_OUT
- U11 pad 4: (no net) -> /V-
- U11 pad 5: (no net) -> GND
- U11 pad 6: /GND -> /CH4_GAIN_FB
- U11 pad 7: (no net) -> /CH4_OUT_DRIVE
- U11 pad 8: (no net) -> /V+
- U12 pad 1: (no net) -> /CH5_BUF_DRIVE
- U12 pad 2: /CH6_GAIN_OUT -> /CH5_BUF_DRIVE
- U12 pad 3: (no net) -> /CH5_GAIN_OUT
- U12 pad 4: (no net) -> /V-
- U12 pad 5: (no net) -> GND
- U12 pad 6: /GND -> /CH5_GAIN_FB
- U12 pad 7: (no net) -> /CH5_OUT_DRIVE
- U12 pad 8: (no net) -> /V+
- U13 pad 2: (no net) -> /CH6_BUF_DRIVE
- U13 pad 3: (no net) -> /CH6_GAIN_OUT
- U14 pad 1: /V+ -> (no net)
- U14 pad 2: /V+ -> (no net)
- U14 pad 3: /GND -> (no net)
- U14 pad 4: /EN_CTRL -> (no net)
- U14 pad 5: /SS_U14 -> (no net)
- U14 pad 6: /+12V -> (no net)
- U14 pad 7: /GND -> (no net)
- U15 pad 1: /GND -> GND
- U2 pad 1: (no net) -> /CH1_RX_OUT
- U2 pad 2: (no net) -> /CH1_INV_IN
- U2 pad 3: /CH2_HOT_IN -> /CH1_HOT_IN
- U2 pad 4: (no net) -> /V-
- U2 pad 5: /CH2_SUMNODE -> GND
- U2 pad 6: /GND -> /CH1_SUMNODE
- U2 pad 7: /CH2_GAIN_OUT -> /CH1_GAIN_OUT
- U2 pad 8: (no net) -> /V+
- U3 pad 1: (no net) -> /CH2_RX_OUT
- U3 pad 2: (no net) -> /CH2_INV_IN
- U3 pad 3: /CH3_HOT_IN -> /CH2_HOT_IN
- U3 pad 4: (no net) -> /V-
- U3 pad 5: /CH3_SUMNODE -> GND
- U3 pad 6: /GND -> /CH2_SUMNODE
- U3 pad 7: /CH3_GAIN_OUT -> /CH2_GAIN_OUT
- U3 pad 8: (no net) -> /V+
- U4 pad 1: (no net) -> /CH3_RX_OUT
- U4 pad 2: (no net) -> /CH3_INV_IN
- U4 pad 3: /CH4_HOT_IN -> /CH3_HOT_IN
- U4 pad 4: (no net) -> /V-
- U4 pad 5: /CH4_SUMNODE -> GND
- U4 pad 6: /GND -> /CH3_SUMNODE
- U4 pad 7: /CH4_GAIN_OUT -> /CH3_GAIN_OUT
- U4 pad 8: (no net) -> /V+
- U5 pad 1: (no net) -> /CH4_RX_OUT
- U5 pad 2: (no net) -> /CH4_INV_IN
- U5 pad 3: /CH5_HOT_IN -> /CH4_HOT_IN
- U5 pad 4: (no net) -> /V-
- U5 pad 5: /CH5_SUMNODE -> GND
- U5 pad 6: /GND -> /CH4_SUMNODE
- U5 pad 7: /CH5_GAIN_OUT -> /CH4_GAIN_OUT
- U5 pad 8: (no net) -> /V+
- U6 pad 1: (no net) -> /CH5_RX_OUT
- U6 pad 2: (no net) -> /CH5_INV_IN
- U6 pad 3: /CH6_HOT_IN -> /CH5_HOT_IN
- U6 pad 4: (no net) -> /V-
- U6 pad 5: /CH6_SUMNODE -> GND
- U6 pad 6: /GND -> /CH5_SUMNODE
- U6 pad 7: /CH6_GAIN_OUT -> /CH5_GAIN_OUT
- U6 pad 8: (no net) -> /V+
- U7 pad 1: (no net) -> /CH6_RX_OUT
- U7 pad 2: /CH1_GAIN_OUT -> /CH6_INV_IN
- U7 pad 3: (no net) -> /CH6_HOT_IN
- U7 pad 4: (no net) -> /V-
- U7 pad 5: (no net) -> GND
- U7 pad 6: /GND -> /CH6_SUMNODE
- U7 pad 7: (no net) -> /CH6_GAIN_OUT
- U7 pad 8: (no net) -> /V+
- U8 pad 1: (no net) -> /CH1_BUF_DRIVE
- U8 pad 2: /CH2_GAIN_OUT -> /CH1_BUF_DRIVE
- U8 pad 3: (no net) -> /CH1_GAIN_OUT
- U8 pad 4: (no net) -> /V-
- U8 pad 5: (no net) -> GND
- U8 pad 6: /GND -> /CH1_GAIN_FB
- U8 pad 7: (no net) -> /CH1_OUT_DRIVE
- U8 pad 8: (no net) -> /V+
- U9 pad 1: (no net) -> /CH2_BUF_DRIVE
- U9 pad 2: /CH3_GAIN_OUT -> /CH2_BUF_DRIVE
- U9 pad 3: (no net) -> /CH2_GAIN_OUT
- U9 pad 4: (no net) -> /V-
- U9 pad 5: (no net) -> GND
- U9 pad 6: /GND -> /CH2_GAIN_FB
- U9 pad 7: (no net) -> /CH2_OUT_DRIVE
- U9 pad 8: (no net) -> /V+
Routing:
- added copper zone on B.Cu, net GND
- added copper zone on F.Cu, net GND
- removed copper zone on B.Cu, net /GND
- removed copper zone on F.Cu, net /GND

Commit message: Fix Q1-Q7 SOT-23 footprint, U14 pad-net injection, exact template matching
- Add Package_TO_SOT_SMD:SOT-23 to EXTRA_FOOTPRINTS (BSS138 is 3-pin, not 5-pin)
- Fix template matching: exact short-name match before substring fallback
- Fix pad-net injection for unquoted pad names (SOIC127P600X175-9N)
- Fix outer pad regex: consume inter-group whitespace in pad block matching

Validation: 0 ERRORS, 0 WARNINGS, 18/18 checks passed
DRC: 0 shorts, 18 courtyard/clearance (power zone), 499 unconnected (pre-routing)
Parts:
- Q1, Q2, Q3, Q4, Q5, Q6, Q7: footprint Package_TO_SOT_SMD:SOT-23-5 -> SOT-23
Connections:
- U14 pad 1: (no net) -> /V+
- U14 pad 2: (no net) -> /V+
- U14 pad 3: (no net) -> /V+
- U14 pad 4: (no net) -> GND
- U14 pad 5: (no net) -> /EN_CTRL
- U14 pad 6: (no net) -> /SS_U14
- U14 pad 7: (no net) -> /+12V
- U14 pad 8: (no net) -> /+12V
- U14 pad 9: (no net) -> GND
